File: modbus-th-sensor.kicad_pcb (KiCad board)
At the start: 2 copper layers, 42 parts, among them J1 Screw Terminal, J2 FTDI Serial, J3 ICSP, Q1 AO3401A, SW2 TERM, SW3 Node ID, U1 ATmega328P-A, U2 SHT4x, U3 SP3485EN, U5 AP63203WU, Y1 8MHz

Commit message: Finished routing main board
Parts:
- removed C15: 0.1uF, Capacitor_SMD:C_0402_1005Metric
- removed D4: SM712, Package_TO_SOT_SMD:SOT-23
- removed Q1: AO3401A, Package_TO_SOT_SMD:SOT-23
- removed the R1 at (143.1, 58.9)
- removed SW2: TERM, Button_Switch_SMD:SW_DIP_SPSTx01_Slide_6.7x4.1mm_W8.61mm_P2.54mm_LowProfile
- removed SW3: Node ID, Button_Switch_SMD:SW_DIP_SPSTx04_Slide_6.7x11.72mm_W8.61mm_P2.54mm_LowProfile
- removed U2: SHT4x, Sensor_Humidity:Sensirion_DFN-4_1.5x1.5mm_P0.8mm_SHT4x_NoCentralPad
- added J4: Sensor Board, Connector_PinSocket_2.54mm:PinSocket_1x05_P2.54mm_Horizontal, F.Cu at (144.9, 100.4)
- added J5: I2C, Connector_JST:JST_PH_B4B-PH-K_1x04_P2.00mm_Vertical, F.Cu at (179.5, 118.5)
- added R6: 10K, Resistor_SMD:R_0603_1608Metric, F.Cu at (164.5, 90.0)
- C1: footprint Capacitor_SMD:CP_Elec_6.3x5.8 -> Capacitor_THT:CP_Radial_D6.3mm_P2.50mm
- C13: footprint Capacitor_SMD:C_0603_1608Metric -> Capacitor_SMD:C_0402_1005Metric
- C5, C6: footprint Capacitor_SMD:C_0603_1608Metric -> Capacitor_SMD:C_1206_3216Metric
- D1: value SMAJ18CA -> SMAJ24CA
- D2: value 10V -> SS210; footprint Diode_SMD:D_SOD-123 -> Diode_SMD:D_SMA
- F1: value 0.75A -> 0.5A; footprint Fuse:Fuse_1206_3216Metric -> Capacitor_THT:C_Disc_D8.0mm_W5.0mm_P5.00mm
- J1: footprint Connector_Phoenix_MC:PhoenixContact_MCV_1,5_4-G-3.5_1x04_P3.50mm_Vertical -> Kefa HT396:Kefa_HT396R-3.96-04P_1x04_P3.96mm_Horizontal
- JP1: value Jumper_2_Open -> Terminate
- L1: renamed from L2; footprint Inductor_SMD:L_1812_4532Metric -> Inductor_SMD:L_Sunlord_SWPA4030S
- R2: renamed from R3; value 330R -> 1K
- R4, R5: value 4.7k -> 10K
- U3: value SP3485EN -> THVD2410DR
- moved J3 74.1 mm to (121.8, 114.5), turned to 180 degrees
- moved R1 52.2 mm to (172.0, 103.5)
- moved JP1 50.4 mm to (167.0, 77.5), turned to 180 degrees
- moved U3 46.6 mm to (169.5, 88.5)
- moved C12 43.1 mm to (131.6, 111.6), turned to -90 degrees
- moved J1 42.9 mm to (144.8, 74.1), turned to 0 degrees
- moved C13 41.0 mm to (175.0, 106.5), turned to 180 degrees
- moved C11 38.1 mm to (130.0, 111.5), turned to -90 degrees
- moved U1 37.6 mm to (132.0, 105.0), turned to -90 degrees
- moved R2 36.1 mm to (128.0, 116.5), turned to -90 degrees
- moved C10 35.5 mm to (132.4, 98.6), turned to 90 degrees
- moved F1 35.2 mm to (136.0, 75.0), turned to 180 degrees
- moved J2 33.6 mm to (179.5, 93.7), turned to 0 degrees
- moved C3 33.2 mm to (131.0, 91.2), turned to 0 degrees
- moved D3 33.0 mm to (127.0, 119.5)
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- renumbered R2 to R1, R6 to R3
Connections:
- net Net-(D2-K) renamed /VIN_PROT
- C13 pad 1: Net-(J2-Pin_1) -> Net-(J2-Pin_6)
- D1 pad 2: Net-(D1-A2) -> /VIN_FUSED
- D2 pad 2: Net-(D2-A) -> /VIN_FUSED
- F1 pad 2: Net-(D1-A2) -> /VIN_FUSED
- J2 pad 1: Net-(J2-Pin_1) -> GND
- J2 pad 2: RXD -> GND
- J2 pad 3: TXD -> +3.3V
- J2 pad 4: +3.3V -> RXI
- J2 pad 5: GND -> TXO
- J2 pad 6: GND -> Net-(J2-Pin_6)
- JP1 pad 1: Net-(JP1-A) -> A
- JP1 pad 2: A -> Net-(JP1-B)
- R3 pad 2: Net-(R6-Pad2) -> Net-(JP1-B)
- R4 pad 2: SDA -> RXI
- R5 pad 2: SCL -> RXEN
- U1 pad 1: TXEN -> RXEN
- U1 pad 10: ID2 -> unconnected-(U1-PD6-Pad10)
- U1 pad 11: ID3 -> unconnected-(U1-PD7-Pad11)
- U1 pad 2: ID0 -> unconnected-(U1-PD4-Pad2)
- U1 pad 26: unconnected-(U1-PC3-Pad26) -> INT
- U1 pad 30: RXD -> RXI
- U1 pad 31: TXD -> TXO
- U1 pad 32: RXEN -> TXEN
- U1 pad 9: ID1 -> unconnected-(U1-PD5-Pad9)
- U3 pad 1: RXD -> RXI
- U3 pad 4: TXD -> TXO
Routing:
- net +3.3V: track 0.00 -> 168.6 mm
- net RXI: track 0.00 -> 61.9 mm, vias 0 -> 3
- net RESET: track 0.00 -> 61.5 mm, vias 0 -> 3
- net TXO: track 0.00 -> 55.3 mm, vias 0 -> 2
- net SDA: track 0.00 -> 54.8 mm
- net A: track 0.00 -> 54.1 mm
- net SCL: track 0.00 -> 52.9 mm
- net GND: track 0.00 -> 44.1 mm, vias 0 -> 19
- net RXEN: track 0.00 -> 39.6 mm, vias 0 -> 2
- net TXEN: track 0.00 -> 37.5 mm, vias 0 -> 2
- net B: track 0.00 -> 33.2 mm
- net Vin: track 0.00 -> 21.7 mm
- net INT: track 0.00 -> 17.9 mm, vias 0 -> 1
- net SDO: track 0.00 -> 17.8 mm
- net SCK: track 0.00 -> 14.8 mm, vias 0 -> 1
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- added copper zone on F.Cu, net +3.3V
- added copper zone on F.Cu, net /VIN_PROT
- added copper zone on F.Cu, net GND
- added copper zone on F.Cu, net Net-(U5-SW)
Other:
- board outline added: 68 x 66 mm
- board text added: "MCU"
- board text added: "Power"
- board text added: "RS-485"
- board text added: "Sensor board"

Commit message: Main board tidy ups - Move U5 FB track away from SW node, BST pad and L1 - Add extra GND vias - Move R1 (RESET pull-up) next to U1 - Include J5 in the BOM, consistent with other hand-fitted connectors
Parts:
- moved R1 31.0 mm to (141.0, 103.5)
- moved C13 0.98 mm to (176.0, 106.5)
- moved D3 0.07 mm to (127.1, 119.5)
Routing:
- net +3.3V: track 168.6 -> 177.1 mm
- net RESET: track 61.5 -> 62.5 mm
- net Net-(J2-Pin_6): track 4.06 -> 3.08 mm
- net GND: track 44.1 -> 44.2 mm, vias 19 -> 26

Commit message: Moved crystal closer to the microcontroller
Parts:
- moved Y1 5.49 mm to (124.0, 100.0)
- moved C7 4.54 mm to (120.0, 98.0), turned to 180 degrees
- moved C8 4.21 mm to (120.0, 101.5), turned to 180 degrees
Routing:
- net Net-(U1-XTAL1/PB6): track 13.5 -> 10.8 mm
- net Net-(U1-XTAL2/PB7): track 10.6 -> 8.99 mm
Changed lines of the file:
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@@
 	(footprint "Crystal:Crystal_SMD_5032-2Pin_5.0x3.2mm"
 		(layer "F.Cu")
-		(at 119.5 96.85 90)
+		(at 124 100 90)
 		(descr "SMD2520/2, Crystal, 5.0x3.2mm package, SMD, http://www.icbase.com/File/PDF/HKC/HKC00061008.pdf")
 		(property "Reference" "Y1"
@@
 	(footprint "Capacitor_SMD:C_0603_1608Metric"
 		(layer "F.Cu")
-		(at 123.275 98.85)
+		(at 120 101.5 180)
 		(descr "Capacitor SMD 0603 (1608 Metric), square (rectangular) end terminal, IPC-7351 nominal, (Body size source: IPC-SM-782 page 76, https://www.pcb-3d.com/wordpress/wp-content/uploads/ipc-sm-782a_amendment_1_and_2.pdf)")
 		(tags "capacitor")
 		(property "Reference" "C8"
-			(at -0.601868 -1.548684 0)
+			(at 0 -1.548684 0)
 			(layer "F.SilkS")
 			(effects
@@
 		)
 		(property "LCSC" "C1653"
-			(at 0 0 0)
+			(at 0 0 180)
 			(unlocked yes)
 			(layer "F.Fab")
@@
 		(duplicate_pad_numbers_are_jumpers no)
 		(fp_line
-			(start -0.14058 -0.51)
-			(end 0.14058 -0.51)
+			(start -0.14058 0.51)
+			(end 0.14058 0.51)
 			(stroke
 				(width 0.12)
@@
 		)
 		(fp_line
-			(start -0.14058 0.51)
-			(end 0.14058 0.51)
+			(start -0.14058 -0.51)
+			(end 0.14058 -0.51)
 			(stroke
 				(width 0.12)
@@
 		)
 		(pad "1" smd roundrect
-			(at -0.775 0)
+			(at -0.775 0 180)
 			(size 0.9 0.95)
 			(layers "F.Cu" "F.Mask" "F.Paste")
@@
 		)
 		(pad "2" smd roundrect
-			(at 0.775 0)
+			(at 0.775 0 180)
 			(size 0.9 0.95)
 			(layers "F.Cu" "F.Mask" "F.Paste")
@@
 	(footprint "Capacitor_SMD:C_0603_1608Metric"
 		(layer "F.Cu")
-		(at 123.275 94.85)
+		(at 120 98 180)
 		(descr "Capacitor SMD 0603 (1608 Metric), square (rectangular) end terminal, IPC-7351 nominal, (Body size source: IPC-SM-782 page 76, https://www.pcb-3d.com/wordpress/wp-content/uploads/ipc-sm-782a_amendment_1_and_2.pdf)")
 		(tags "capacitor")
 		(property "Reference" "C7"
-			(at -0.601868 -1.51075 0)
+			(at 0 -1.51075 0)
 			(layer "F.SilkS")
 			(effects
@@
 		)
 		(property "LCSC" "C1653"
-			(at 0 0 0)
+			(at 0 0 180)
 			(unlocked yes)
 			(layer "F.Fab")
@@
 		(duplicate_pad_numbers_are_jumpers no)
 		(fp_line
-			(start -0.14058 -0.51)
-			(end 0.14058 -0.51)
+			(start -0.14058 0.51)
+			(end 0.14058 0.51)
 			(stroke
 				(width 0.12)
@@
 		)
 		(fp_line
-			(start -0.14058 0.51)
-			(end 0.14058 0.51)
+			(start -0.14058 -0.51)
+			(end 0.14058 -0.51)
 			(stroke
 				(width 0.12)
@@
 		)
 		(pad "1" smd roundrect
-			(at -0.775 0)
+			(at -0.775 0 180)
 			(size 0.9 0.95)
 			(layers "F.Cu" "F.Mask" "F.Paste")
@@
 		)
 		(pad "2" smd roundrect
-			(at 0.775 0)
+			(at 0.775 0 180)
 			(size 0.9 0.95)
 			(layers "F.Cu" "F.Mask" "F.Paste")
@@
 	)
 	(segment
-		(start 124.05 93.565015)
-		(end 124.053177 93.561838)
-		(width 0.5)
-		(layer "F.Cu")
-		(net "GND")
-	)
-	(segment
 		(start 172.48 83.5)
 		(end 172.5 83.52)
@@
 	)
 	(segment
+		(start 118 101.5)
+		(end 119.225 101.5)
+		(width 0.5)
+		(layer "F.Cu")
+		(net "GND")
+	)
+	(segment
 		(start 131.966582 112.033418)
 		(end 131.645827 112.033418)
@@
 	)
 	(segment
-		(start 124.05 94.85)
-		(end 124.05 93.565015)
-		(width 0.5)
-		(layer "F.Cu")
-		(net "GND")
-	)
-	(segment
 		(start 144.7675 80.2325)
 		(end 144.5 80.5)
@@
 	)
 	(segment
-		(start 124.097695 97.590681)
-		(end 124.097695 98.802305)
-		(width 0.5)
-		(layer "F.Cu")
-		(net "GND")
-	)
-	(segment
 		(start 179.5 93.65)
 		(end 179.5 96.19)
@@
 	)
 	(segment
-		(start 131.6 102.25436)
-		(end 131.593911 102.260449)
+		(start 118 98)
+		(end 119.225 98)
 		(width 0.5)
 		(layer "F.Cu")
@@
 	)
 	(segment
-		(start 124.097695 98.802305)
-		(end 124.05 98.85)
+		(start 131.6 102.25436)
+		(end 131.593911 102.260449)
 		(width 0.5)
 		(layer "F.Cu")
@@
 	)
 	(via
-		(at 124.053177 93.561838)
-		(size 0.6)
-		(drill 0.3)
-		(layers "F.Cu" "B.Cu")
-		(free yes)
-		(net "GND")
-	)
-	(via
 		(at 135 91.9)
 		(size 0.6)
@@
 	)
 	(via
-		(at 124.097695 97.590681)
+		(at 118 98)
 		(size 0.6)
 		(drill 0.3)
@@
 	)
 	(via
+		(at 118 101.5)
+		(size 0.6)
+		(drill 0.3)
+		(layers "F.Cu" "B.Cu")
+		(free yes)
+		(net "GND")
+	)
+	(via
 		(at 135 93.5)
 		(size 0.6)
@@
 	)
 	(segment
-		(start 124.4875 100.8375)
-		(end 122.5 98.85)
+		(start 123.5 101.5)
+		(end 120.775 101.5)
 		(width 0.2)
 		(layer "F.Cu")
@@
 	)
 	(segment
-		(start 129.2 100.8375)
-		(end 124.4875 100.8375)
+		(start 124 101.85)
+		(end 123.85 101.85)
 		(width 0.2)
 		(layer "F.Cu")
@@
 	)
 	(segment
-		(start 122.35 98.7)
-		(end 122.5 98.85)
+		(start 125.0125 100.8375)
+		(end 124 101.85)
 		(width 0.2)
 		(layer "F.Cu")
@@
 	)
 	(segment
-		(start 119.5 98.7)
-		(end 122.35 98.7)
+		(start 123.85 101.85)
+		(end 123.5 101.5)
 		(width 0.2)
 		(layer "F.Cu")
@@
 	)
 	(segment
-		(start 119.5 95)
-		(end 122.35 95)
+		(start 129.2 100.8375)
+		(end 125.0125 100.8375)
 		(width 0.2)
 		(layer "F.Cu")
-		(net "Net-(U1-XTAL1{slash}PB6)")
+		(net "Net-(U1-XTAL2{slash}PB7)")
 	)
 	(segment
-		(start 130 100.100001)
-		(end 125.524999 95.625)
+		(start 120.925 98.15)
+		(end 120.775 98)
 		(width 0.2)
 		(layer "F.Cu")
@@
 	)
 	(segment
-		(start 125.524999 95.625)
-		(end 123.275 95.625)
+		(start 130 100.100001)
+		(end 128.049999 98.15)
 		(width 0.2)
 		(layer "F.Cu")
@@
 	)
 	(segment
-		(start 122.35 95)
-		(end 122.5 94.85)
+		(start 128.049999 98.15)
+		(end 124 98.15)
 		(width 0.2)
 		(layer "F.Cu")
@@
 	)
 	(segment
-		(start 123.275 95.625)
-		(end 122.5 94.85)
+		(start 124 98.15)
+		(end 120.925 98.15)
 		(width 0.2)
 		(layer "F.Cu")

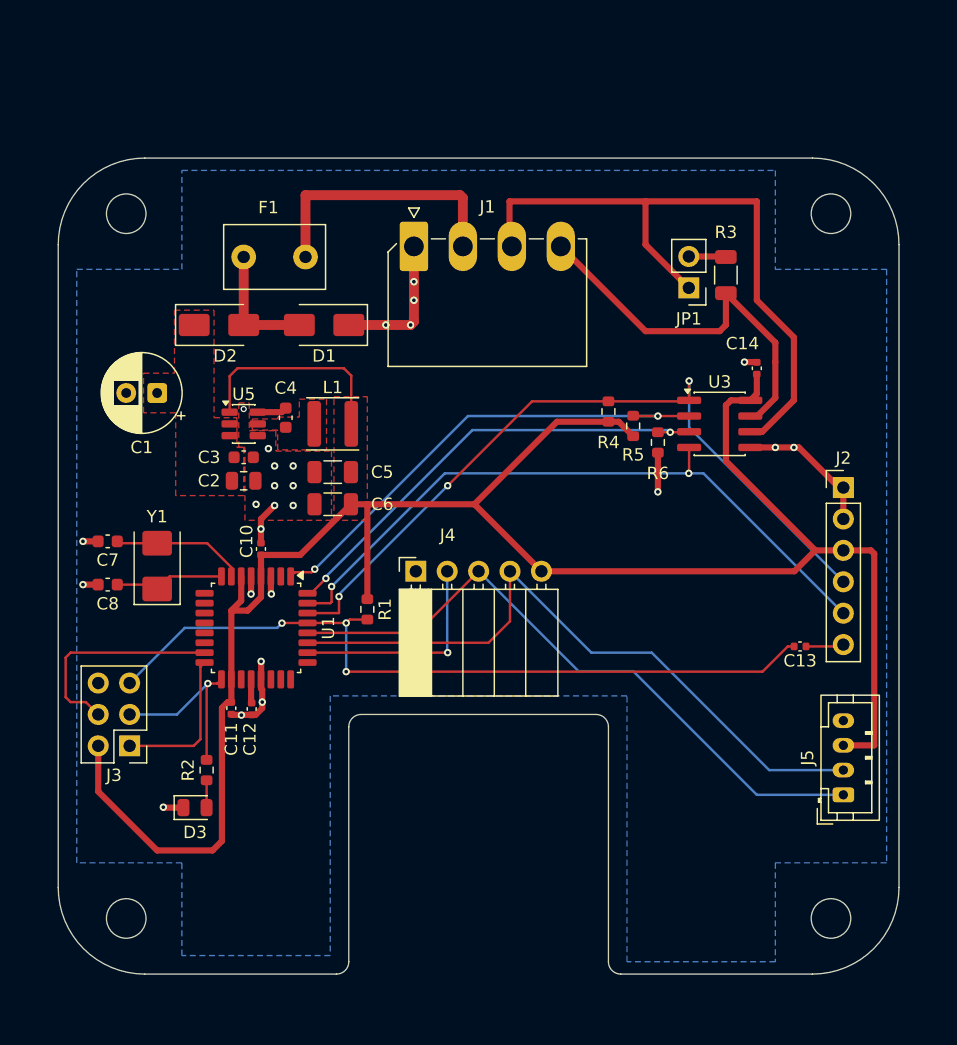
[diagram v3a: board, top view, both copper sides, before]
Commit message: Re-worked main board for the Camdenboss CBRS01 series of enclosures - New 73.32 x 73.32 mm outline, with M2.5 mounting holes - Moved the sensor notch so the breakout's mounting hole sits on the lid's centre post - Added back the Unit ID jumper header
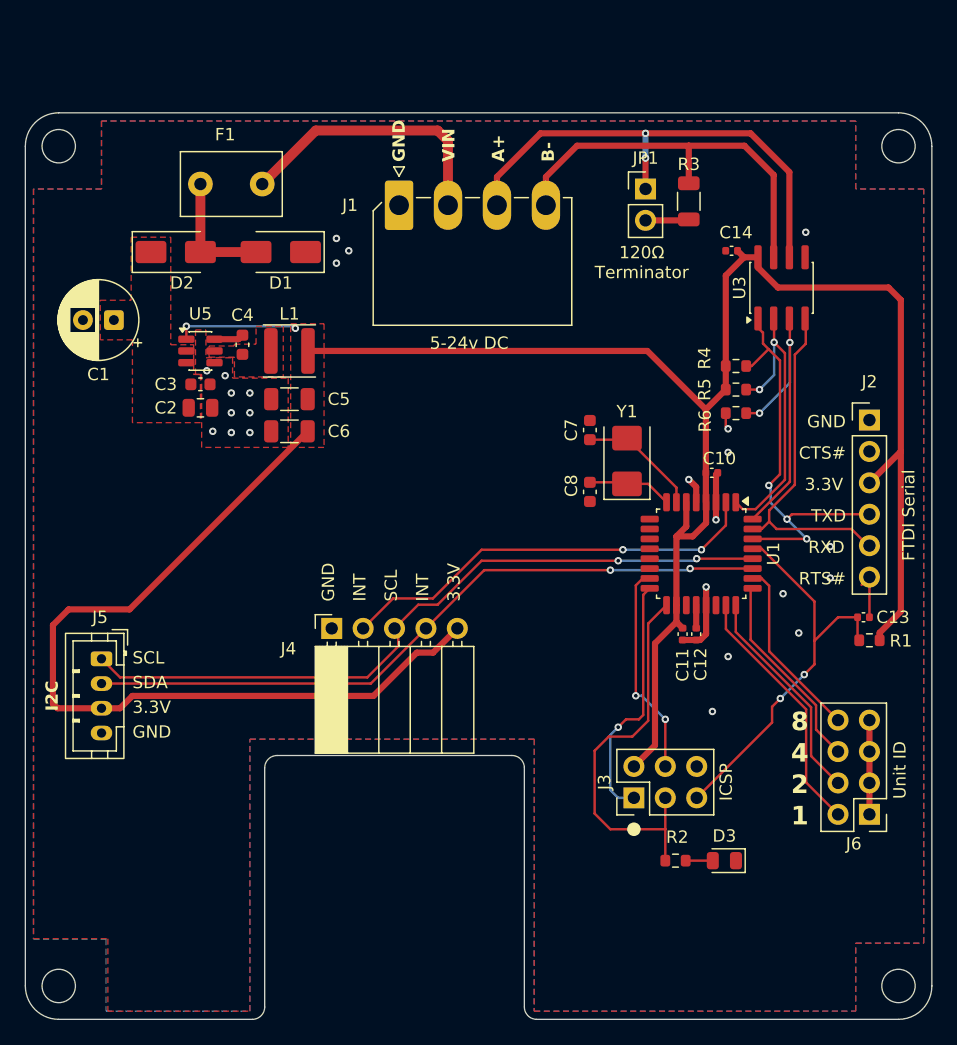
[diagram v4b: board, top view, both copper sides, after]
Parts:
- added J6: Unit ID, Connector_PinHeader_2.54mm:PinHeader_2x04_P2.54mm_Vertical, F.Cu at (181.6, 120.1)
- H1, H2, H3, H4: footprint MountingHole:MountingHole_3.2mm_M3 -> MountingHole:MountingHole_2.7mm_M2.5
- moved J5 61.0 mm to (119.5, 107.5), turned to -90 degrees
- moved D3 43.0 mm to (169.9, 123.8), turned to 180 degrees
- moved J3 41.0 mm to (162.6, 118.7), turned to 90 degrees
- moved R1 40.7 mm to (181.6, 106.0), turned to 180 degrees
- moved C7 40.0 mm to (159.0, 89.0), turned to 90 degrees
- moved C8 39.7 mm to (159.0, 94.0), turned to -90 degrees
- moved Y1 38.9 mm to (162.0, 91.5)
- moved R2 38.6 mm to (165.9, 123.8), turned to 0 degrees
- moved C11 37.0 mm to (166.5, 105.5)
- moved C10 37.0 mm to (168.9, 92.5), turned to 0 degrees
- moved U1 36.5 mm to (168.0, 99.0)
- moved C12 36.5 mm to (167.6, 105.5)
- moved U3 12.1 mm to (174.5, 77.5), turned to 90 degrees
- moved R4 11.0 mm to (170.8, 83.8), turned to 0 degrees
- moved C14 9.72 mm to (170.5, 74.5), turned to 180 degrees
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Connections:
- U1 pad 2: unconnected-(U1-PD4-Pad2) -> INT
- U1 pad 23: unconnected-(U1-PC0-Pad23) -> ID1
- U1 pad 24: unconnected-(U1-PC1-Pad24) -> ID2
- U1 pad 25: unconnected-(U1-PC2-Pad25) -> ID3
- U1 pad 26: INT -> ID4
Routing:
- net +3.3V: track 177.1 -> 209.7 mm, vias 0 -> 2
- net RESET: track 62.5 -> 32.8 mm, vias 3 -> 2
- net RXI: track 61.9 -> 32.9 mm
- net TXO: track 55.3 -> 28.0 mm, vias 2 -> 0
- net GND: track 44.1 -> 20.8 mm, vias 26 -> 24
- net ID1: track 0.00 -> 20.7 mm
- net ID2: track 0.00 -> 17.8 mm
- net SCK: track 14.8 -> 31.7 mm, vias 1 -> 0
- net INT: track 17.9 -> 34.7 mm, vias 1 -> 2
- net ID3: track 0.00 -> 16.0 mm
- net RXEN: track 39.6 -> 24.0 mm
- net ID4: track 0.00 -> 14.8 mm
- net A: track 54.1 -> 40.1 mm, vias 0 -> 2
- net TXEN: track 37.5 -> 25.2 mm
- net SDI: track 12.3 -> 20.4 mm, vias 0 -> 1
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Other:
- board size 68 x 66 mm -> 73.3 x 73.3 mm
- board text added: "1"
- board text added: "120Ω Terminator"
- board text added: "2"
- board text added: "3.3V"
- board text added: "4"
- board text added: "5-24v DC"
- board text added: "8"
- board text added: "A+"
- board text added: "B-"
- board text added: "CTS#"
- board text added: "GND"
- board text added: "INT"
- board text added: "RTS#"
- board text added: "RXD"
- board text added: "SCL"
- board text added: "SDA"
- board text added: "TXD"
- board text added: "VIN"

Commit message: Moved buck converter FB back to the front layer Minor value and label changes.
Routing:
- net +3.3V: track 209.7 -> 215.3 mm, vias 2 -> 0
- net GND: vias 24 -> 26
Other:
- board text added: "5-24V DC"
- board text removed: "5-24v DC"
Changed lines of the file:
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@@
 	)
 	(paper "A4")
+	(title_block
+		(title "Modbus Room Sensor")
+		(date "2026-10-21")
+		(rev "2")
+		(company "aelius labs")
+	)
 	(layers
 		(0 "F.Cu" signal)
@@
 		(35 "F.Fab" user)
 		(33 "B.Fab" user)
-		(39 "User.1" user)
-		(41 "User.2" user)
-		(43 "User.3" user)
-		(45 "User.4" user)
 	)
 	(setup
@@
 			(at 5.94 10.8 0)
 			(layer "F.Fab")
+			(hide yes)
 			(effects
 				(font
@@
 		(tags "Through hole pin header THT 2x04 2.54mm double row")
 		(property "Reference" "J6"
-			(at 1.27 -2.38 0)
+			(at 1.27 10.225 0)
 			(layer "F.SilkS")
 			(effects
@@
 		(layer "F.SilkS")
 	)
+	(gr_rect
+		(start 176.7825 122.9025)
+		(end 183.8975 129.8275)
+		(stroke
+			(width 0.1)
+			(type solid)
+		)
+		(fill yes)
+		(layer "F.SilkS")
+	)
 	(gr_arc
 		(start 133.699999 118.66)
@@
 		)
 	)
-	(gr_text "5-24v DC"
+	(gr_text "5-24V DC"
 		(at 146.05 82.55 0)
 		(layer "F.SilkS")
@@
 		)
 	)
-	(gr_text "INT"
+	(gr_text "SDA"
 		(at 146.05 102.87 90)
 		(layer "F.SilkS")
@@
 	)
 	(via
-		(at 131.5 89.2)
+		(at 131.5 88.9)
 		(size 0.6)
 		(drill 0.3)
@@
 	)
 	(via
-		(at 130 87.6)
+		(at 130.048 87.376)
 		(size 0.6)
 		(drill 0.3)
@@
 	)
 	(via
-		(at 130 86)
+		(at 130.048 86)
 		(size 0.6)
 		(drill 0.3)
@@
 	)
 	(via
+		(at 130 79.9)
+		(size 0.6)
+		(drill 0.3)
+		(layers "F.Cu" "B.Cu")
+		(net "GND")
+	)
+	(via
 		(at 139.5 74.5)
 		(size 0.6)
@@
 	)
 	(via
-		(at 131.5 87.6)
+		(at 131.5 87.376)
 		(size 0.6)
 		(drill 0.3)
@@
 	)
 	(via
-		(at 130 89.2)
+		(at 133.1 79.9)
+		(size 0.6)
+		(drill 0.3)
+		(layers "F.Cu" "B.Cu")
+		(net "GND")
+	)
+	(via
+		(at 130.048 88.9)
 		(size 0.6)
 		(drill 0.3)
@@
 	)
 	(segment
+		(start 126.3625 79.6)
+		(end 127.1625 78.8)
+		(width 0.2)
+		(layer "F.Cu")
+		(net "+3.3V")
+	)
+	(segment
 		(start 119.5 111.5)
 		(end 115.945 111.5)
@@
 	)
 	(segment
+		(start 126.3625 81.65)
+		(end 126.3625 79.6)
+		(width 0.2)
+		(layer "F.Cu")
+		(net "+3.3V")
+	)
+	(segment
 		(start 116.84 103.505)
 		(end 121.77 103.505)
@@
 	)
 	(segment
-		(start 126.3625 81.65)
-		(end 126.3625 80.6)
+		(start 136.2 79.6)
+		(end 136.2 82.6)
 		(width 0.2)
 		(layer "F.Cu")
@@
 	)
 	(segment
+		(start 135.4 78.8)
+		(end 136.2 79.6)
+		(width 0.2)
+		(layer "F.Cu")
+		(net "+3.3V")
+	)
+	(segment
 		(start 167.315021 97.6)
 		(end 166 97.6)
@@
 	)
 	(segment
-		(start 183.15 77.47)
-		(end 184.15 78.47)
-		(width 0.5)
-		(layer "F.Cu")
-		(net "+3.3V")
-	)
-	(via
-		(at 135.179058 80.769415)
-		(size 0.6)
-		(drill 0.3)
-		(layers "F.Cu" "B.Cu")
-		(free yes)
-		(net "+3.3V")
-	)
-	(via
-		(at 126.3625 80.6)
-		(size 0.6)
-		(drill 0.3)
-		(layers "F.Cu" "B.Cu")
-		(net "+3.3V")
-	)
-	(segment
-		(start 126.3625 80.6)
-		(end 135.009643 80.6)
+		(start 127.1625 78.8)
+		(end 135.4 78.8)
 		(width 0.2)
-		(layer "B.Cu")
+		(layer "F.Cu")
 		(net "+3.3V")
 	)
 	(segment
-		(start 135.009643 80.6)
-		(end 135.179058 80.769415)
-		(width 0.2)
-		(layer "B.Cu")
+		(start 183.15 77.47)
+		(end 184.15 78.47)
+		(width 0.5)
+		(layer "F.Cu")
 		(net "+3.3V")
 	)

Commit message: Silkscreen adjustments, added OSHW logos
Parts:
- added REF**: OSHW-Logo_7.5x8mm_SilkScreen, Symbol:OSHW-Logo_7.5x8mm_SilkScreen, F.Cu at (122.9, 125.0)
- added REF**: KiCad-Logo2_8mm_SilkScreen, Symbol:KiCad-Logo2_8mm_SilkScreen, B.Cu at (148.8, 95.0)
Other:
- board text added: "AL100 REV ${REVISION}"
- board text added: "aelius labs"
